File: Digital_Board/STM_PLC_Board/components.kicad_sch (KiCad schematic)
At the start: 36 parts, among them J2 Conn_02x14_Odd_Even, Q1 2N7002, Q2 2N7002, Q3 2N7002, Q4 2N7002, SW1 SW_Push, SW2 SW_DIP_x01, SW3 SW_DIP_x01

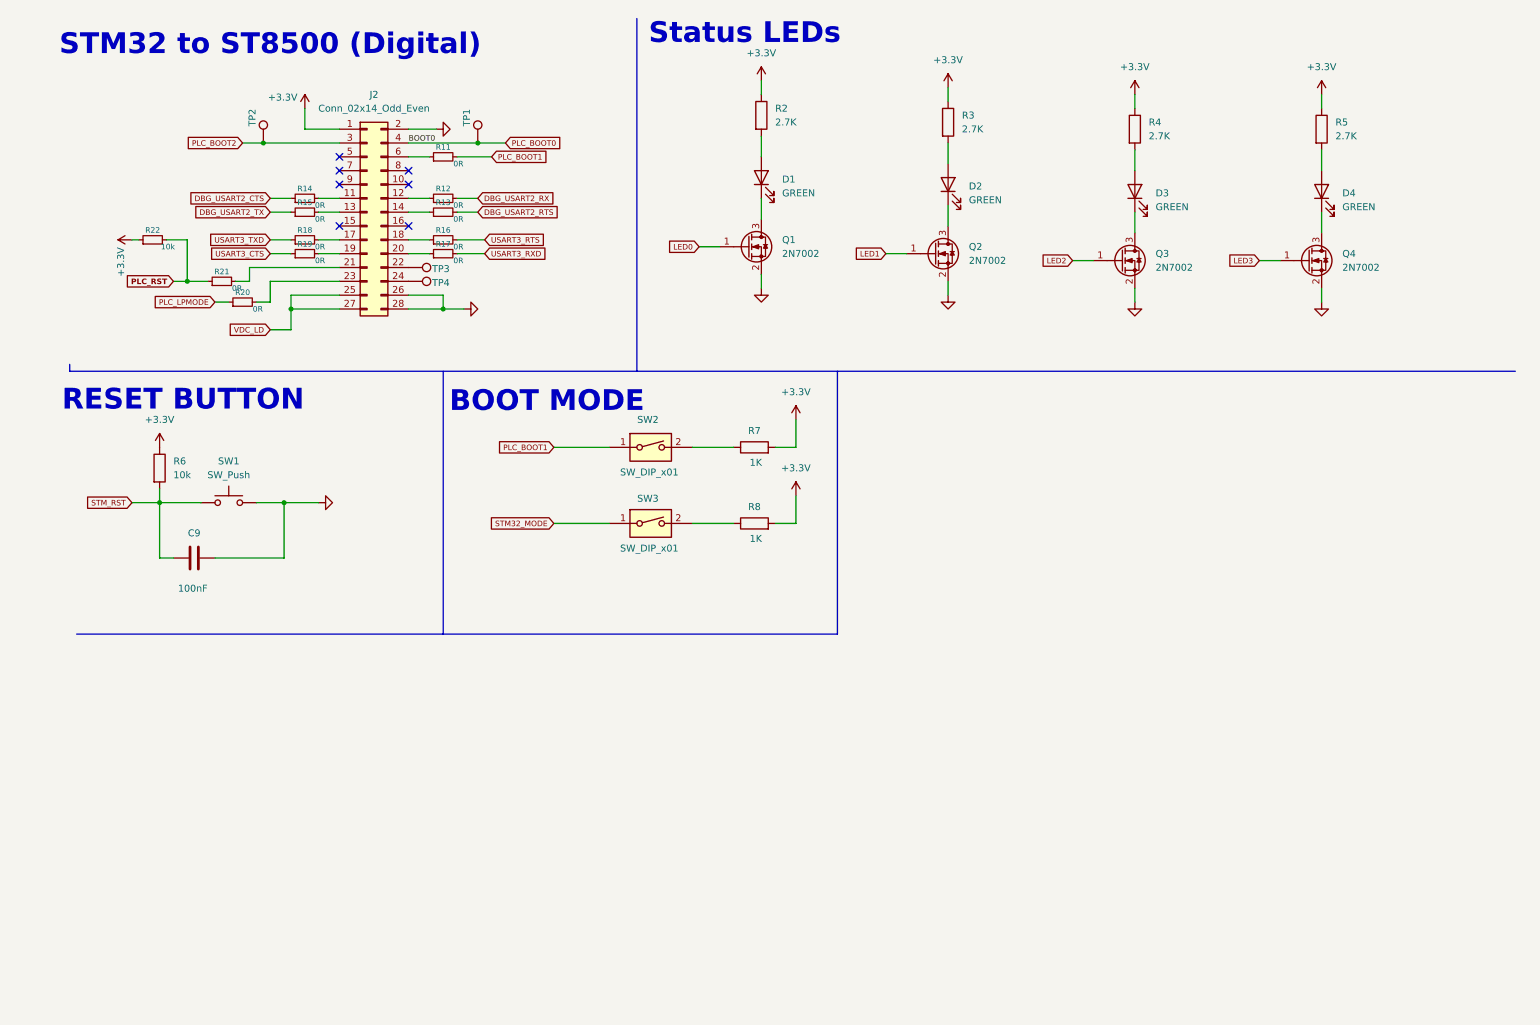
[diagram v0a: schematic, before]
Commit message: STM32 schematic done
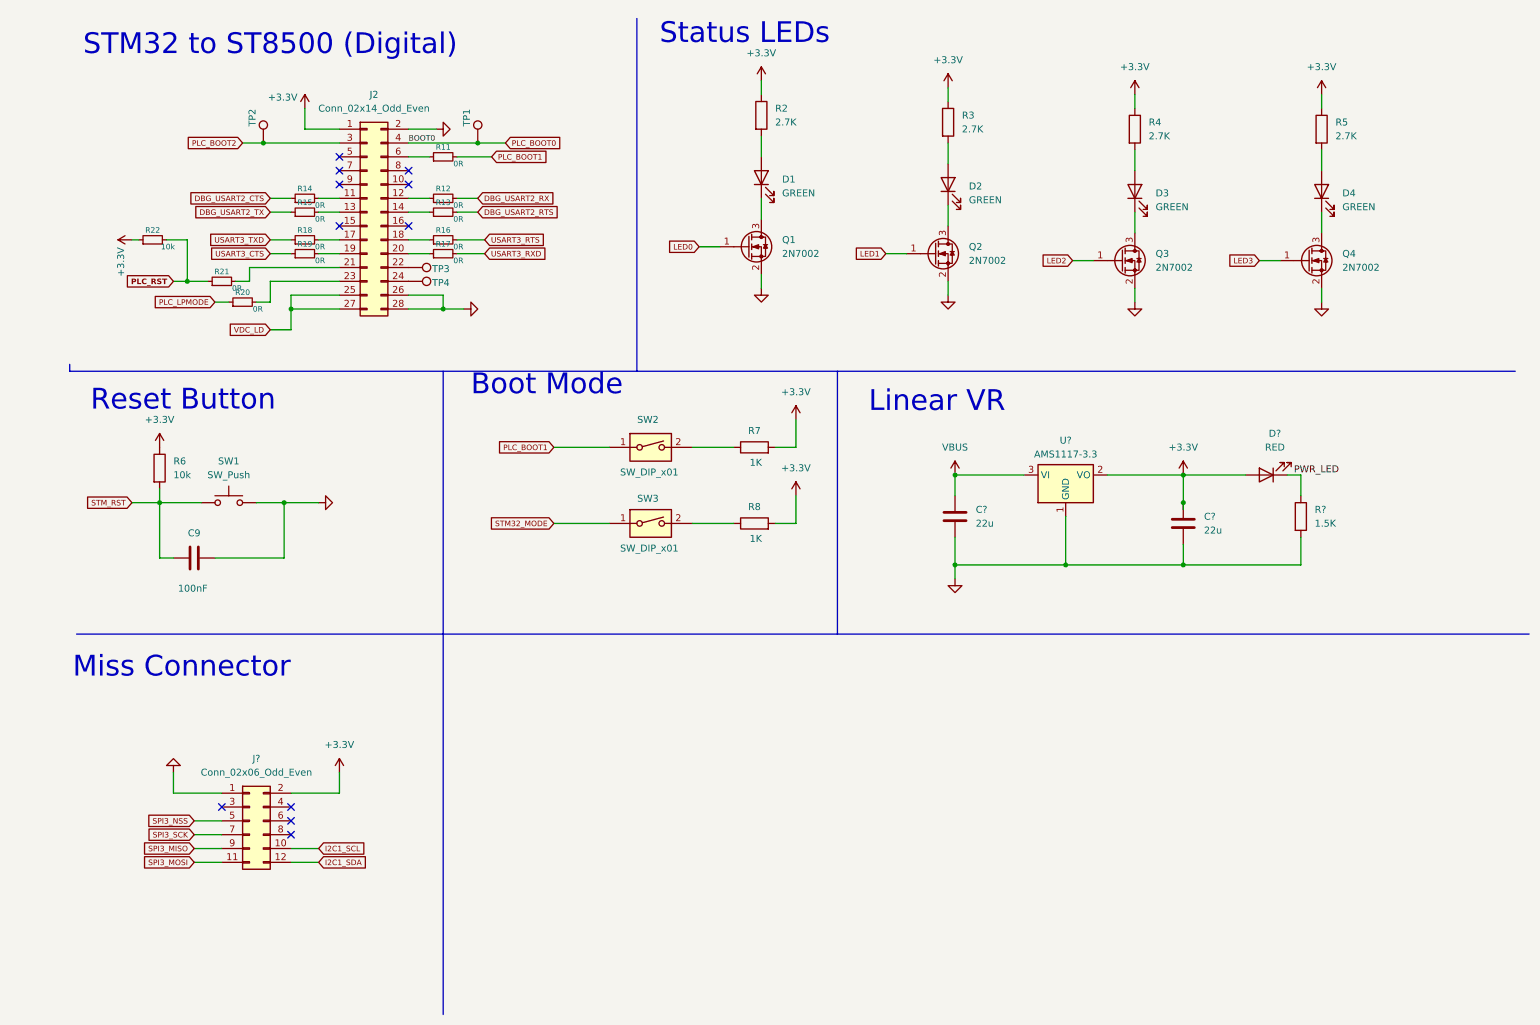
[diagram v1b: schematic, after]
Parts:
- added C? (x2): 22u, symbol Device:C
- added D?: RED, symbol Device:LED
- added J?: Conn_02x06_Odd_Even, symbol Connector_Generic:Conn_02x06_Odd_Even
- added R?: 1.5K, symbol Device:R
- added U?: AMS1117-3.3, Package_TO_SOT_SMD:SOT-223-3_TabPin2, symbol Regulator_Linear:AMS1117-3.3
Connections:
- net +3.3V: now also C?.1, D?.2 (A), J?.2 (Pin_2), U?.2 (VO)
- net GND: now also C?.2, C?.2, J?.1 (Pin_1), R?.2, U?.1 (GND)
- new net I2C1_SCL: J?.10 (Pin_10)
- new net I2C1_SDA: J?.12 (Pin_12)
- new net PWR_LED: D?.1 (K), R?.1
- new net SPI3_MISO: J?.9 (Pin_9)
- new net SPI3_MOSI: J?.11 (Pin_11)
- new net SPI3_NSS: J?.5 (Pin_5)
- new net SPI3_SCK: J?.7 (Pin_7)
- new net VBUS: C?.1, U?.3 (VI)
- no-connect marks 7 -> 11
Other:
- note added: "Boot Mode"
- note added: "Linear VR"
- note added: "Miss Connector"
- note added: "Reset Button"
- note removed: "BOOT MODE"
- note removed: "RESET BUTTON"

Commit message: prez
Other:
- note added: "Misc. Connector"
- note removed: "Miss Connector"
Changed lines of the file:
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@@
 	(generator_version "10.0")
 	(paper "A4")
-	(text "Miss Connector\n"
+	(text "Misc. Connector\n"
 		(exclude_from_sim no)
 		(at 35.814 133.096 0)
